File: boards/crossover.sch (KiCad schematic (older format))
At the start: 62 parts, among them J1 JACK_TRS_6PINS, P1 12-0-12, T1 TRANSFO_3, U1 TL072, U2 TL074, U3 TDA7292, U4 TL074

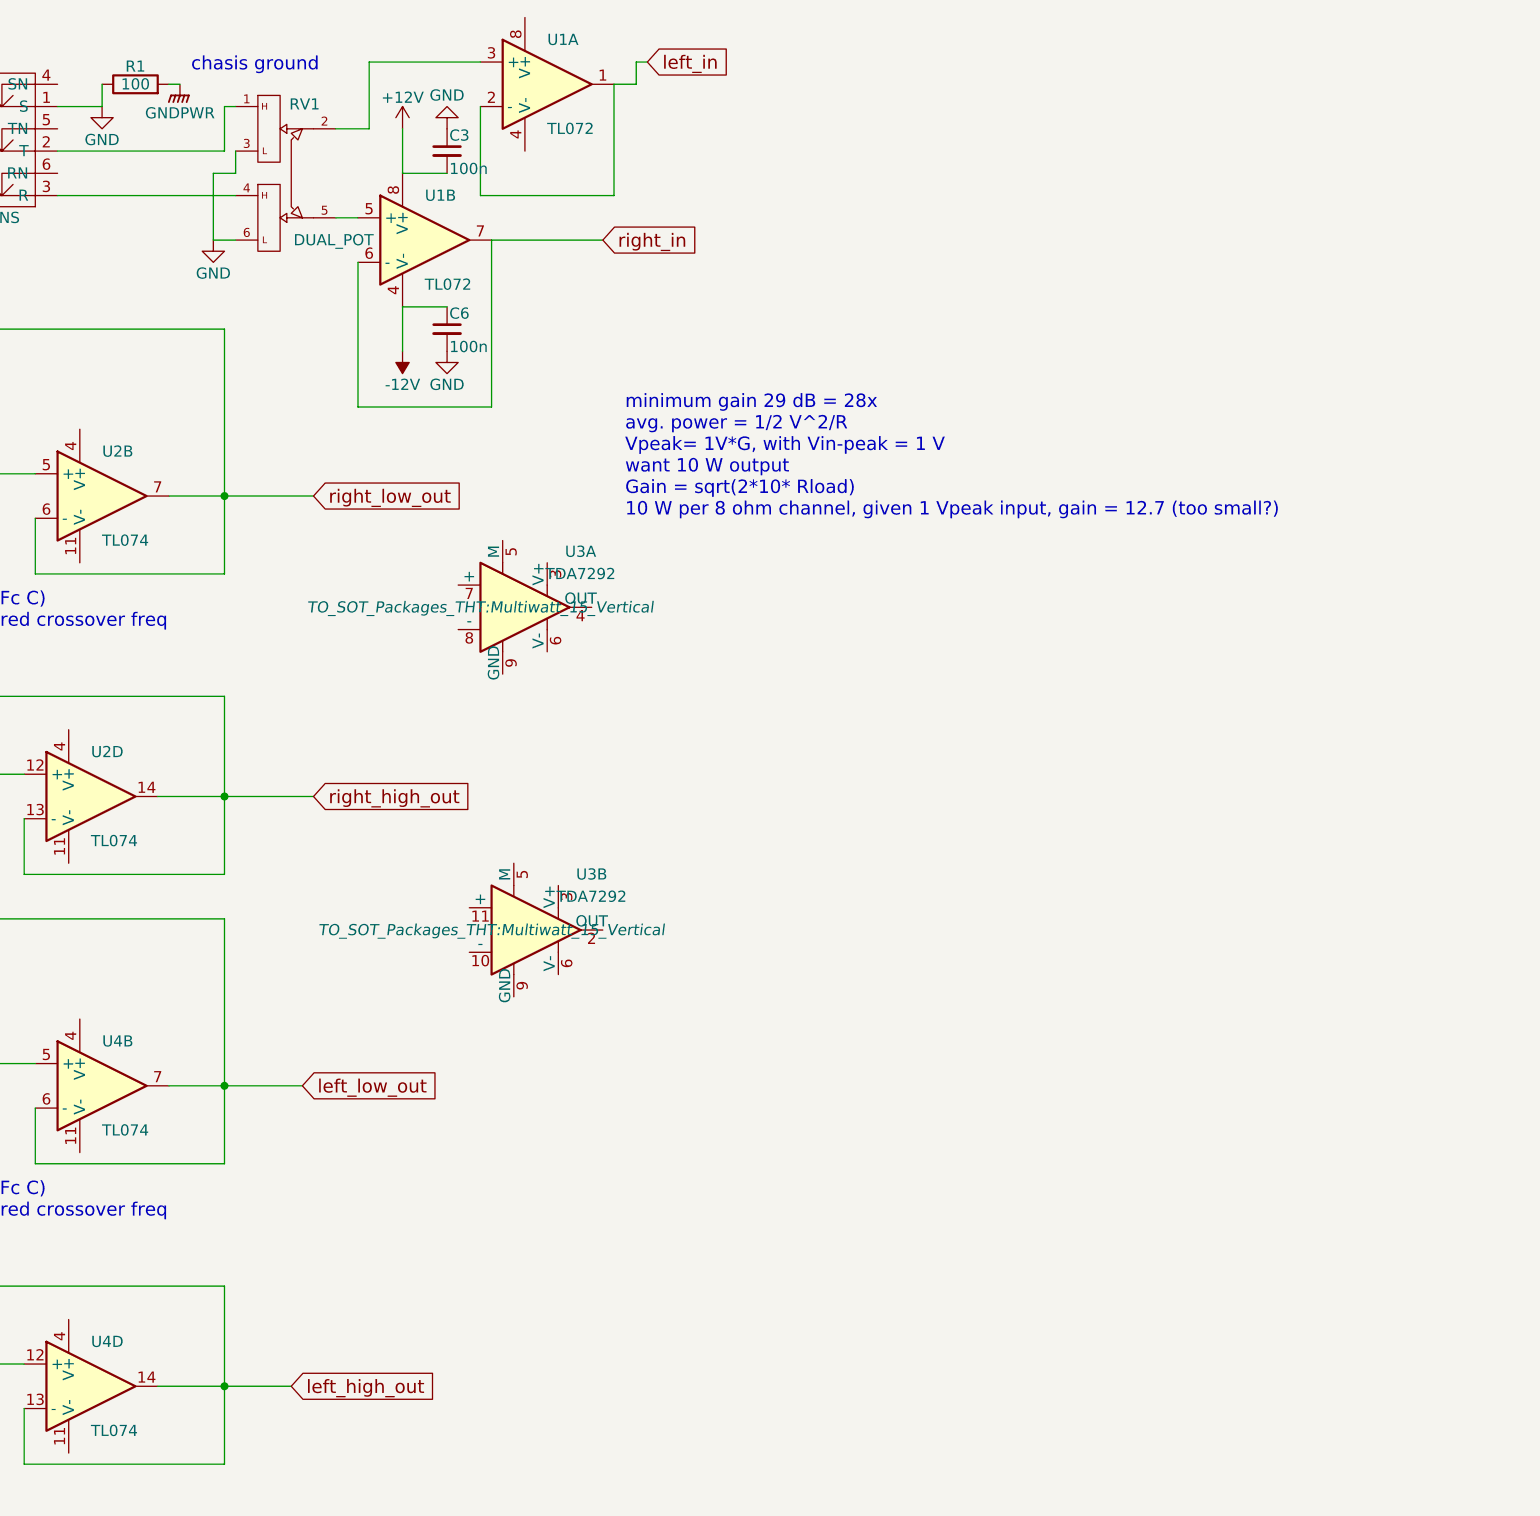
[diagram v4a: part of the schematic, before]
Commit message: first working impedance measurements
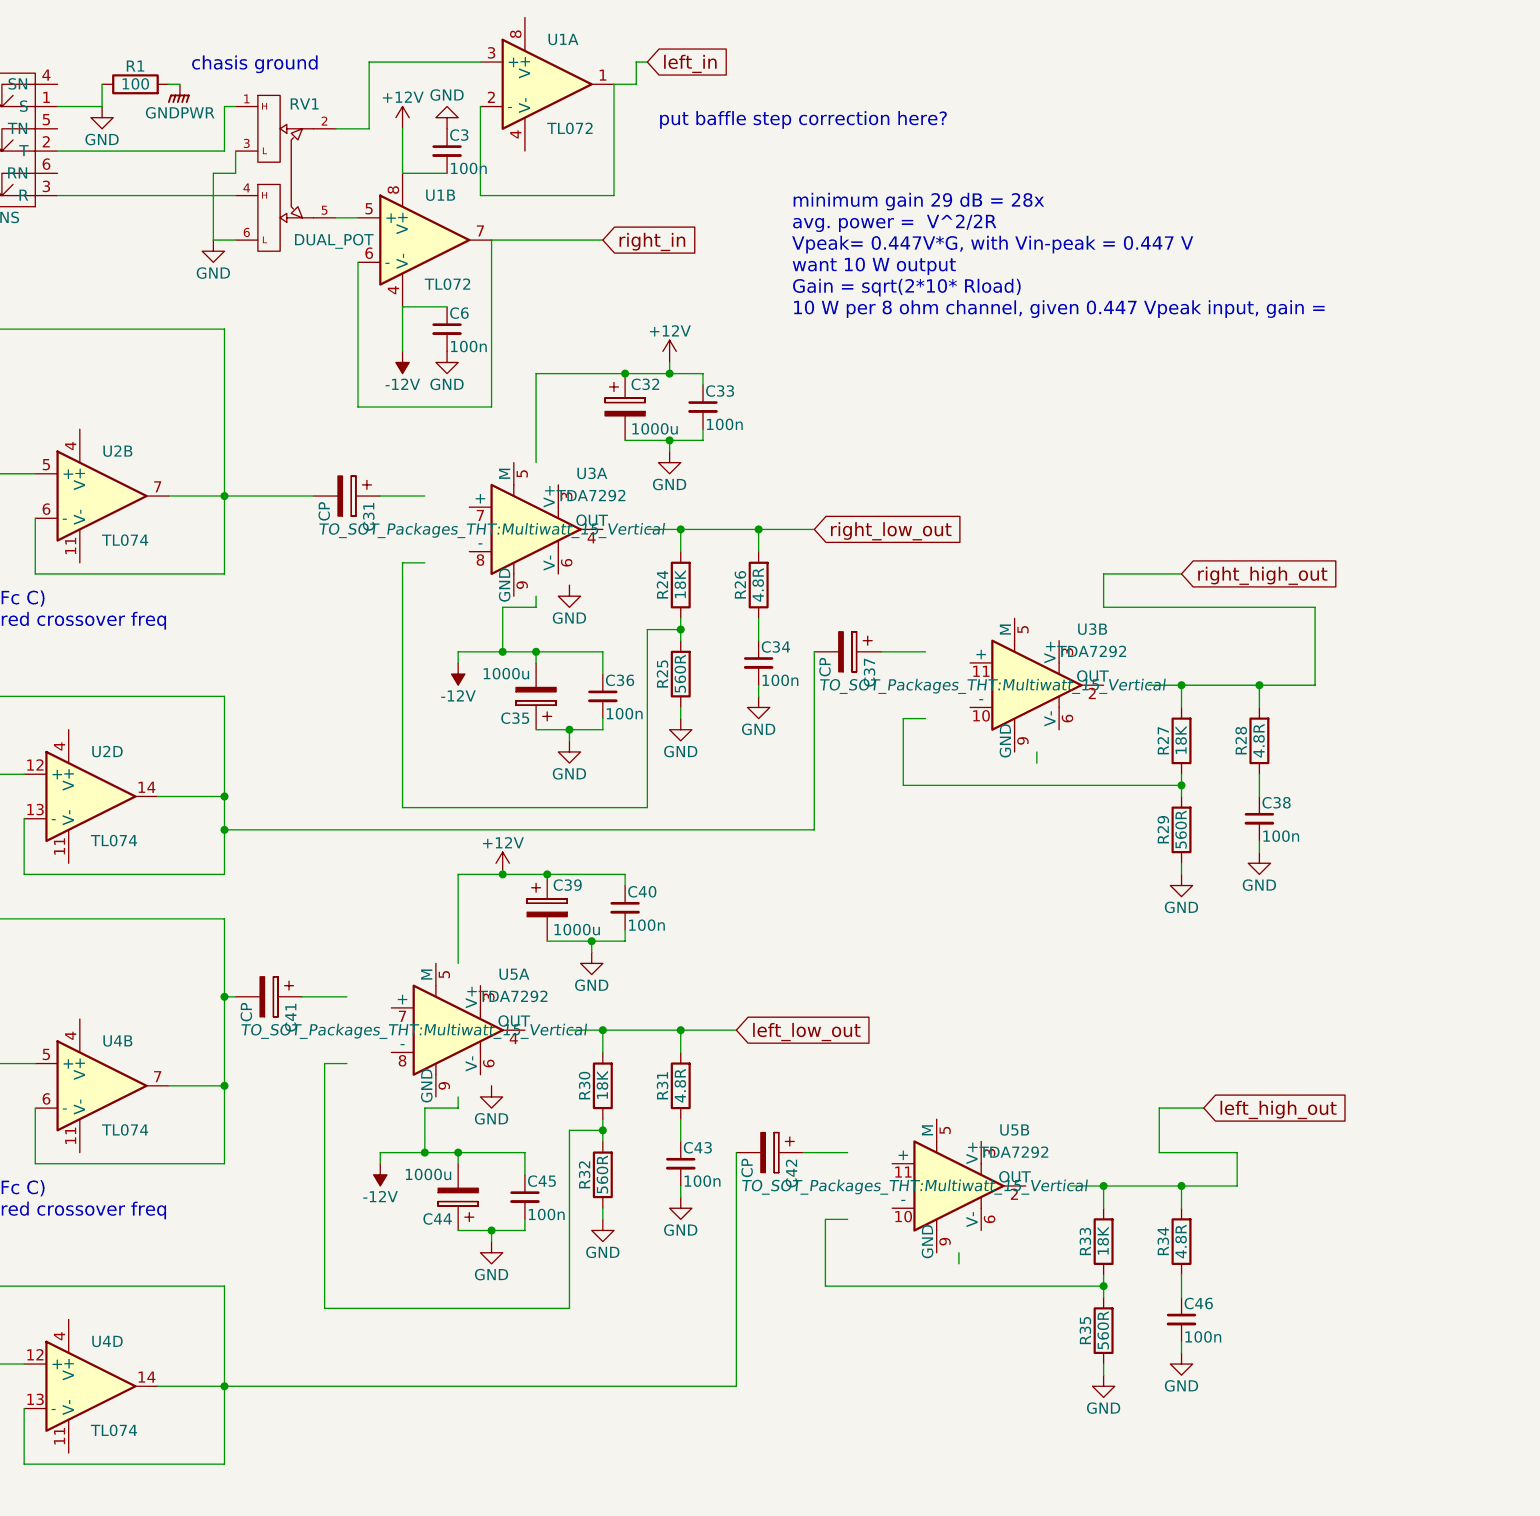
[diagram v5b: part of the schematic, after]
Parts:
- added C31, C37, C41, C42: CP, Capacitors_ThroughHole:C_Radial_D5_L11_P2, symbol CP
- added C32, C35, C39, C44: 1000u, Capacitors_ThroughHole:C_Radial_D10_L20_P5, symbol CP
- added C33, C34, C36, C38, C40, C43, C45, C46: 100n, Capacitors_ThroughHole:C_Disc_D3_P2.5, symbol C_Small
- added R24, R27, R30, R33: 18K, Resistors_ThroughHole:Resistor_Horizontal_RM10mm, symbol R
- added R25, R29, R32, R35: 560R, Resistors_ThroughHole:Resistor_Horizontal_RM10mm, symbol R
- added R26, R28, R31, R34: 4.8R, Resistors_ThroughHole:Resistor_Horizontal_RM10mm, symbol R
- added U5: TDA7292, TO_SOT_Packages_THT:Multiwatt_15_Vertical, symbol TDA7292
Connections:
- wire segments 173 -> 268
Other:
- note added: "minimum gain 29 dB = 28x\navg. power = V^2/2R\nVpeak= 0.447V*G, with Vin-peak = 0.447 V\nwant 10 W output\nGain = sqrt(2*10* Rload)\n10 W per 8 ohm channel, given 0.447 Vpeak input, gain ="
- note added: "put baffle step correction here?"
- note removed: "minimum gain 29 dB = 28x\navg. power = 1/2 V^2/R\nVpeak= 1V*G, with Vin-peak = 1 V\nwant 10 W output\nGain = sqrt(2*10* Rload)\n10 W per 8 ohm channel, given 1 Vpeak input, gain = 12.7 (too small?)"
- moved on the sheet: U3A

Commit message: documentation, pcb updates, some pylint fixes
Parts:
- removed J1: JACK_TRS_6PINS, Socket_Strips:Socket_Strip_Angled_1x06, symbol JACK_TRS_6PINS
- removed R1: 100, Resistors_ThroughHole:Resistor_Horizontal_RM10mm, symbol R
- added P2: CONN_01X03, Terminal_Blocks:TerminalBlock_Pheonix_MKDS1.5-3pol, symbol CONN_01X03
- added P3, P4: CONN_01X04, Terminal_Blocks:TerminalBlock_Pheonix_MKDS1.5-4pol, symbol CONN_01X04
- added R36, R37: 1K, Resistors_ThroughHole:Resistor_Horizontal_RM7mm, symbol R
- added novalue1: connector for dual pot, symbol DUAL_POT
- added novalue2: dual pot, symbol DUAL_POT
- C1: manf# (none) -> K104K15X7RF53L2
- C2: footprint Capacitors_ThroughHole:C_Radial_D16_L31.5_P7.5 -> Capacitors_ThroughHole:C_Radial_D22_L41_P10; manf# (none) -> UVR1H682MRD
- C31: value CP -> 1u; manf# (none) -> 105CKR050M
- C32: manf# (none) -> 108CKS025M
- C37, C41, C42: value CP -> 1u
- C5: footprint Capacitors_ThroughHole:C_Radial_D16_L31.5_P7.5 -> Capacitors_ThroughHole:C_Radial_D22_L41_P10
- C7: manf# (none) -> FG26C0G1H104JNT06
- D1: footprint Diodes_ThroughHole:Diode_Bridge_15.7x15.7 -> Diodes_ThroughHole:Diode_Bridge_18.5x5.5; manf# (none) -> GBU8J-BP
- P1: value 12-0-12 -> CONN_01X03; manf# (none) -> 1935174
- R10, R11, R16, R17, R18, R19, R20, R21, R22, R23, R8, R9: value RH -> R; footprint Resistors_ThroughHole:Resistor_Horizontal_RM10mm -> Resistors_ThroughHole:Resistor_Horizontal_RM7mm
- R12, R13, R14, R15, R5, R6, R7: value RL -> R; footprint Resistors_ThroughHole:Resistor_Horizontal_RM10mm -> Resistors_ThroughHole:Resistor_Horizontal_RM7mm
- R2: manf# (none) -> ROX1SJ1K0
- R4: value RL -> R; footprint Resistors_ThroughHole:Resistor_Horizontal_RM10mm -> Resistors_ThroughHole:Resistor_Horizontal_RM7mm; manf# (none) -> MCMF0W4FF1101A50
- RV1: footprint Pin_Headers:Pin_Header_Straight_2x03 -> Connectors_Molex:Molex_KK-6410-06_06x2.54mm_Straight; manf# (none) -> 640456-6
- T1: manf# (none) -> VPS24-5400
- U1: manf# (none) -> tl072
- U2: manf# (none) -> tl074cn
- U3: manf# (none) -> tda7292
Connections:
- net labels added: +12VAC, -12VAC
- net labels removed: GNDPWR
- wire segments 268 -> 277
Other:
- note added: "1s turn-on delay"
- note added: "Connectors: Pheonix PT series 0.5mm"
- note added: "R=1/(2 pi \sqrt{2} Fc C)\nC= 100nF, Fc=desired crossover freq\ne.g., R = 1.1K, Fc = 1023Hz"
- note added: "Set gain for tweeter and woofer seperately\nthey have different efficiencies"
- note added: "TE MTA-100 series conn."
- note added: "USE KICOST for BOMs!"
- note added: "connect pin 2 to chassis? only if balanced?"
- note added: "minimum gain 29 dB = 28x\navg. power = V^2/2R\nVpeak= 0.447V*G, with Vin-peak = 0.447 V\nwant 10 W output\nGain = sqrt(2*10* Road)\n10 W per 8 ohm channel, given 0.447 Vpeak input, gain ="
- note added: "unbalanced out, if shielded use chassis for shield"
- note removed: "+/-12 V is actually more like 17 V (peak to peak)"
- note removed: "chasis ground"
- note removed: "minimum gain 29 dB = 28x\navg. power = V^2/2R\nVpeak= 0.447V*G, with Vin-peak = 0.447 V\nwant 10 W output\nGain = sqrt(2*10* Rload)\n10 W per 8 ohm channel, given 0.447 Vpeak input, gain ="
- moved on the sheet: C32, C33, C39

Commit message: some board updates
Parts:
- removed R37: 1K, Resistors_ThroughHole:Resistor_Horizontal_RM7mm, symbol R
- added C47: 1000u, Capacitors_ThroughHole:C_Radial_D10_L20_P5, symbol CP
- added C54, C55: 100n, Capacitors_ThroughHole:C_Disc_D3_P2.5, symbol C_Small
- added R48, R50: Rbs1, Resistors_ThroughHole:Resistor_Horizontal_RM7mm, symbol R
- added R49, R51: Rbs2, Resistors_ThroughHole:Resistor_Horizontal_RM7mm, symbol R
- added RV2, RV3: 1K POT, Potentiometers:Potentiometer_Bourns_3339P_Angular_ScrewUp, symbol POT
- R24, R30: value 18K -> 68K
- R25, R32: value 560R -> 1K5
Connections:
- net labels added: 1s_delay, left_tweeter_ph, left_woofer_in, right_tweeter_ph, right_woofer_in
- wire segments 277 -> 285
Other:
- note added: "Baffle Step:\nfeedback R1 || C, then R2 to ground\nf_bs = 1/(R1*C*2*pi)\nR2 = R1/(BS_gain-1)\nfor 6 dB:\nR2 = R1/(2-1)=R1\nfor 3 dB:\nR2 = R1/(\sqrt{2}-1)=R1*2.4142"
- note added: "tweeter fixed gain of 30.4 dB\nwoofer variable 29-33.5 dB gain"
- note removed: "1s turn-on delay"
- note removed: "Set gain for tweeter and woofer seperately\nthey have different efficiencies"
- note removed: "put baffle step correction here?"
- moved on the sheet: R24, R25

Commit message: updated board
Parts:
- removed T1: TRANSFO_3, symbol TRANSFO_3
- added novalue3: HEATSINK FOR TDA7292, TO_SOT_Packages_THT:Multiwatt-11_Vertical_StaggeredType1, symbol TDA7292
- added novalue4: TRANSFO_3, symbol TRANSFO_3
- C54, C55: footprint Capacitors_ThroughHole:C_Disc_D3_P2.5 -> Capacitors_ThroughHole:C_Disc_D6_P5
- U3, U5: footprint TO_SOT_Packages_THT:Multiwatt_15_Vertical -> TO_SOT_Packages_THT:Multiwatt-11_Vertical_StaggeredType1
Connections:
- wire segments 285 -> 284
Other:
- note added: "Design:\n10W in to each 8 ohm driver\n-which means ~~9V RMS and ~~1.1 A RMS each\n-Power supply needs > 4.4 A, ~~5A\n- ~~20W power dissipated in each chip, 10W each driver = 80W\n- 80W/24 V RMS = 3.3 A RMS\n\n1% THD\n-Vs needs +/- 20V (for 6 ohm, 13.5V)\n- 12-0-12 transformer will get ~~+/-17 V (maybe good enough)\n\nResevoir Caps\n- C = Q/V = I*t/V, I is ~~5 A, t = 1/60/2, \n- Supply V rejection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"
- note added: "http://www.signaltransfer.freeuk.com/powerout.htm\ntl07x max V is +/15V\nVp after rectifier = 15V\nVp before rectifier = 17 V (two diode drop off)\nVrms before rectifier = 12 V <- use this transformer\n\nFor one 8 ohm driver:\n15 Vs = ~~8 W per driver for 1% THD (10W for 10%)\nsqrt(10 W * 8 omh) = 8.9 Vrms over driver\n8.9 V rms = 12.6 Vp\nIpk = 12.6/8 = 1.6 A peak <-5 less than Imax = 5A\nEach r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"
- note added: "possible ground loop? audio in and power in both ground?"
- note removed: "Design:\n10W in to each 8 ohm driver\n-which means ~~9V and ~~1.1 A each\n-Power supply needs > 4.4 A, ~~5A\n- 20-25W power dissipated in each chip, 10W each driver = 80-90W\n\n1% THD\n-Vs needs +/- 20V (for 6 ohm, 13.5V)\n- 12-0-12 transformer will get ~~+/-17 V (maybe good enough)\n\nResevoir Caps\n- C = Q/V = I*t/V, I is ~~5 A, t = 1/60/2, \n- Supply V rejection ratio = 75 dB\ngain ~~30 dB, 75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"
- moved on the sheet: C31, C32, C33, C37, C39, C40, C41, C42, C47, R36
